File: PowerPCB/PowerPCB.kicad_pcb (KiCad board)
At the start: 2 copper layers, 41 parts, among them J1 Conn_01x03_Male, J2 Conn_01x10_Male, J5 Conn_01x07_Male, K1 1721081-5, K2 1721081-5, K3 1721081-5, Q1 Q_PMOS_DGS, U1 NCP1117-3.3_SOT223, U2 STM32F413ZHTx, U3 NCP1117-5.0_SOT223, U4 MCP2562-E-P, U5 MCP2562-E-P

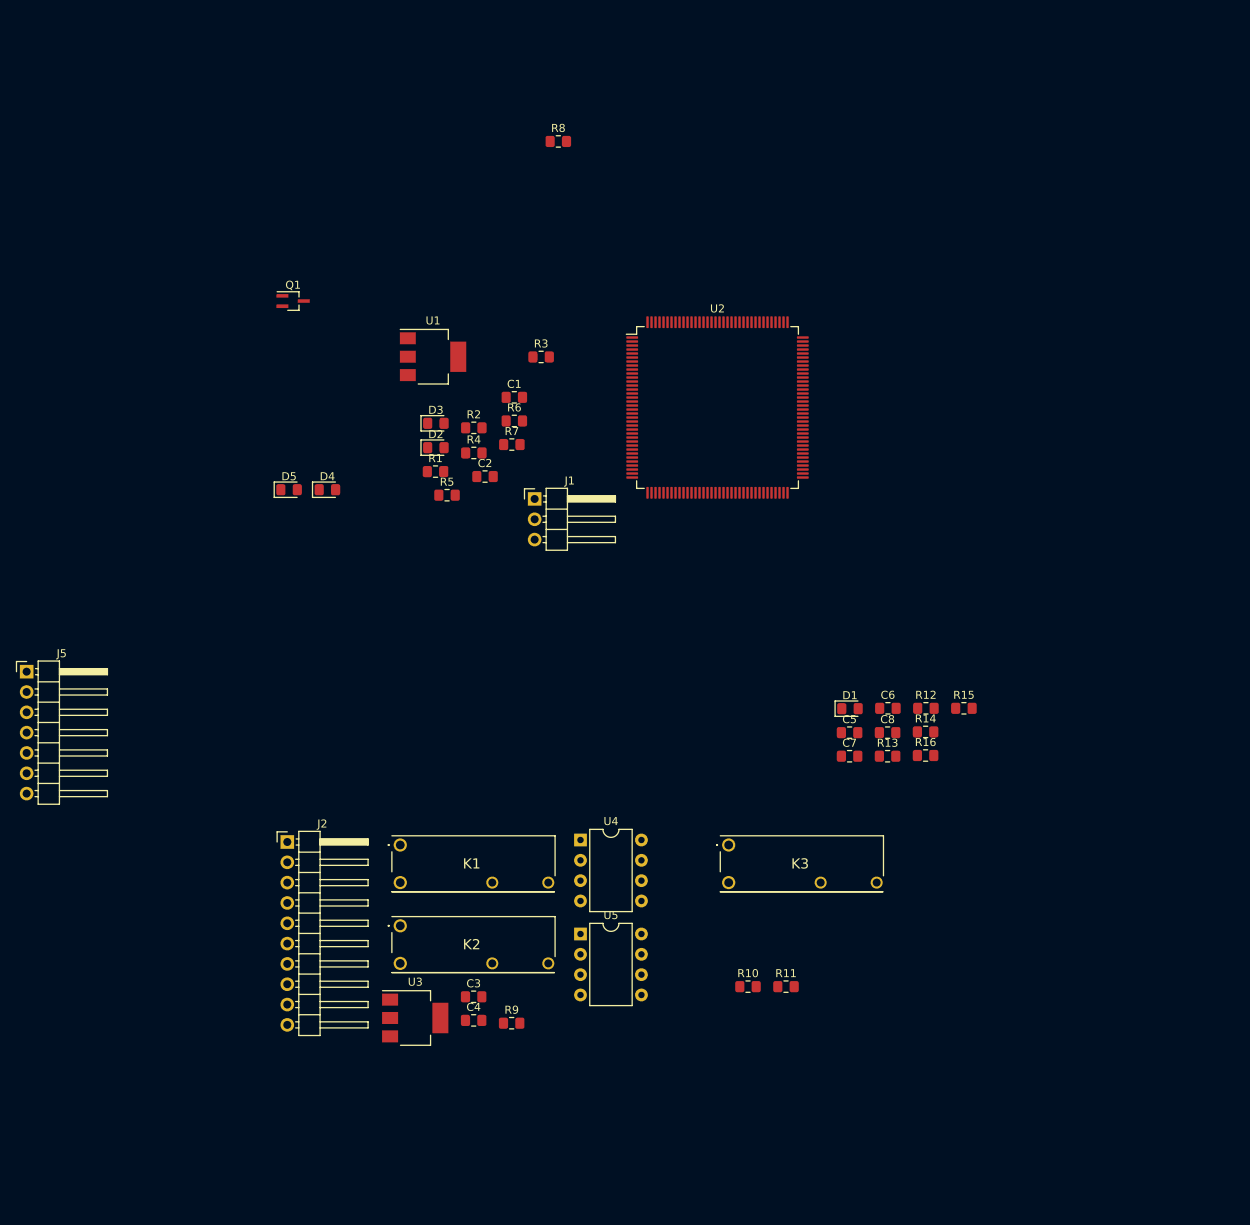
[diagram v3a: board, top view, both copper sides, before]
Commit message: Create new Daichi branch, made PCB layout up to the tracks
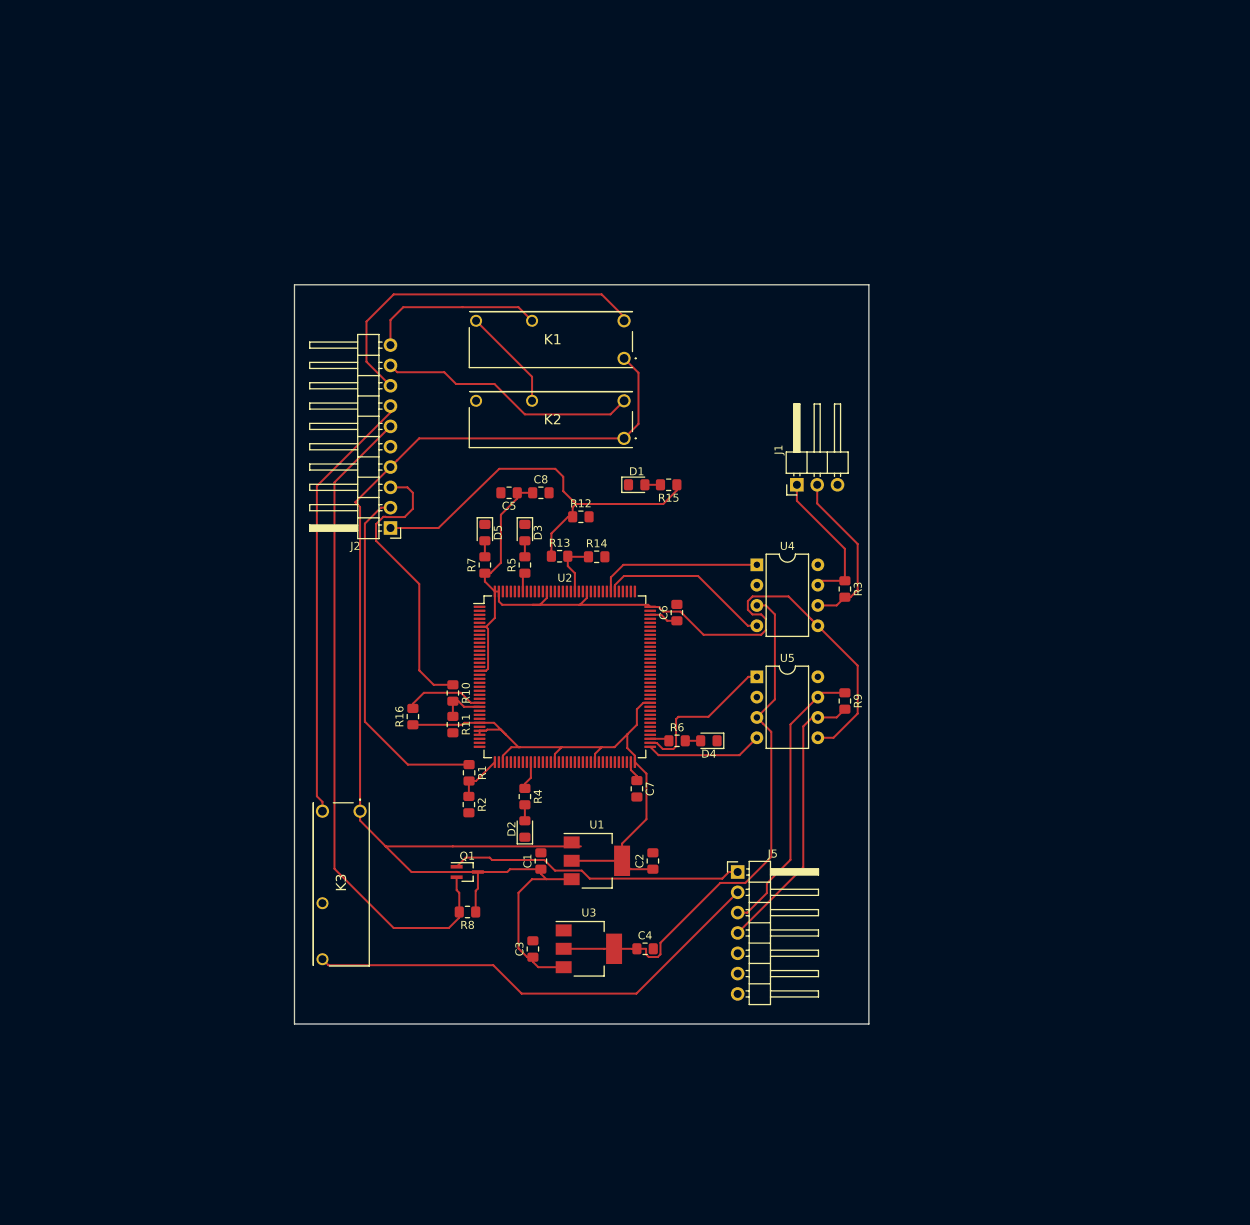
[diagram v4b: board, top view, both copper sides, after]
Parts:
- moved R8 97.0 mm to (354.8, 243.4), turned to 180 degrees
- moved J5 92.3 mm to (388.6, 238.4)
- moved Q1 74.6 mm to (354.8, 238.4)
- moved K2 67.0 mm to (374.4, 184.2), turned to 180 degrees
- moved K1 66.9 mm to (374.4, 174.2), turned to 180 degrees
- moved U1 66.3 mm to (371.0, 237.0)
- moved R16 64.3 mm to (348.0, 219.0), turned to 90 degrees
- moved C1 58.1 mm to (364.0, 237.0), turned to 90 degrees
- moved R9 57.9 mm to (402.0, 217.0), turned to 270 degrees
- moved D4 57.1 mm to (385.0, 222.0), turned to 180 degrees
- moved R11 53.0 mm to (353.0, 220.0), turned to 270 degrees
- moved C8 52.7 mm to (364.0, 191.0)
- moved C2 52.4 mm to (378.0, 237.0), turned to 90 degrees
- moved C5 52.1 mm to (360.0, 191.0), turned to 180 degrees
- moved R10 52.0 mm to (353.0, 216.0), turned to 270 degrees
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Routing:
- net VCC_3.3: track 0.00 -> 181.8 mm
- net VCC_12: track 0.00 -> 166.2 mm
- net /Fan/FanPWM: track 0.00 -> 82.6 mm
- net VCC_5: track 0.00 -> 67.5 mm
- net /Fan/Fan-: track 0.00 -> 58.9 mm
- net /Fan/FanCtrl: track 0.00 -> 54.7 mm
- net DCDC_ON: track 0.00 -> 51.2 mm
- net Net-(J2-Pad8): track 0.00 -> 44.5 mm
- net AUX+: track 0.00 -> 44.0 mm
- net /Fan/Fan+: track 0.00 -> 37.0 mm
- net DCDC+: track 0.00 -> 36.0 mm
- net MAIN_CAN_HI: track 0.00 -> 35.4 mm
- net MAIN_CAN_LO: track 0.00 -> 35.3 mm
- net Net-(J2-Pad9): track 0.00 -> 32.4 mm
- net Net-(J2-Pad10): track 0.00 -> 22.2 mm
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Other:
- board outline added: 71.8 x 92.4 mm

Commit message: small changes to tracks
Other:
- net class Default: trace_width 0.25 -> 1.27
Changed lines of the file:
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@@
   )
   (setup
-    (last_trace_width 0.25)
+    (last_trace_width 1.27)
     (trace_clearance 0.2)
     (zone_clearance 0.508)
@@
   (net_class Default "This is the default net class."
     (clearance 0.2)
-    (trace_width 0.25)
+    (trace_width 1.27)
     (via_dia 0.8)
     (via_drill 0.4)
@@
   (segment (start 374.4 184.2) (end 376.2 182.4) (width 0.25) (layer F.Cu) (net 2))
   (segment (start 376.2 182.4) (end 376.2 176) (width 0.25) (layer F.Cu) (net 2))
-  (segment (start 345.2 187.78) (end 340.8 192.18) (width 0.25) (layer F.Cu) (net 2))
   (segment (start 362.9 239.3) (end 364.675 239.3) (width 0.25) (layer F.Cu) (net 2))
   (segment (start 361.2 241) (end 362.9 239.3) (width 0.25) (layer F.Cu) (net 2))
@@
   (segment (start 356.13 238.4) (end 359.8 238.4) (width 0.25) (layer F.Cu) (net 2))
   (segment (start 359.8 238.4) (end 360.15 238.05) (width 0.25) (layer F.Cu) (net 2))
-  (segment (start 341.4 192.78) (end 341.4 230.8) (width 0.25) (layer F.Cu) (net 2))
-  (segment (start 340.8 192.18) (end 341.4 192.78) (width 0.25) (layer F.Cu) (net 2))
   (segment (start 374.4 184.2) (end 348.78 184.2) (width 0.25) (layer F.Cu) (net 2))
   (segment (start 346.049999 186.930001) (end 345.2 187.78) (width 0.25) (layer F.Cu) (net 2))
   (segment (start 348.78 184.2) (end 346.049999 186.930001) (width 0.25) (layer F.Cu) (net 2))
+  (segment (start 340.8 230.2) (end 341.4 230.8) (width 0.25) (layer F.Cu) (net 2))
+  (segment (start 345.2 187.78) (end 340.8 192.18) (width 0.25) (layer F.Cu) (net 2))
+  (segment (start 340.8 192.18) (end 340.8 230.2) (width 0.25) (layer F.Cu) (net 2))
   (segment (start 362 230) (end 362 232) (width 0.25) (layer F.Cu) (net 3))
   (segment (start 362 197) (end 362 199) (width 0.25) (layer F.Cu) (net 4))

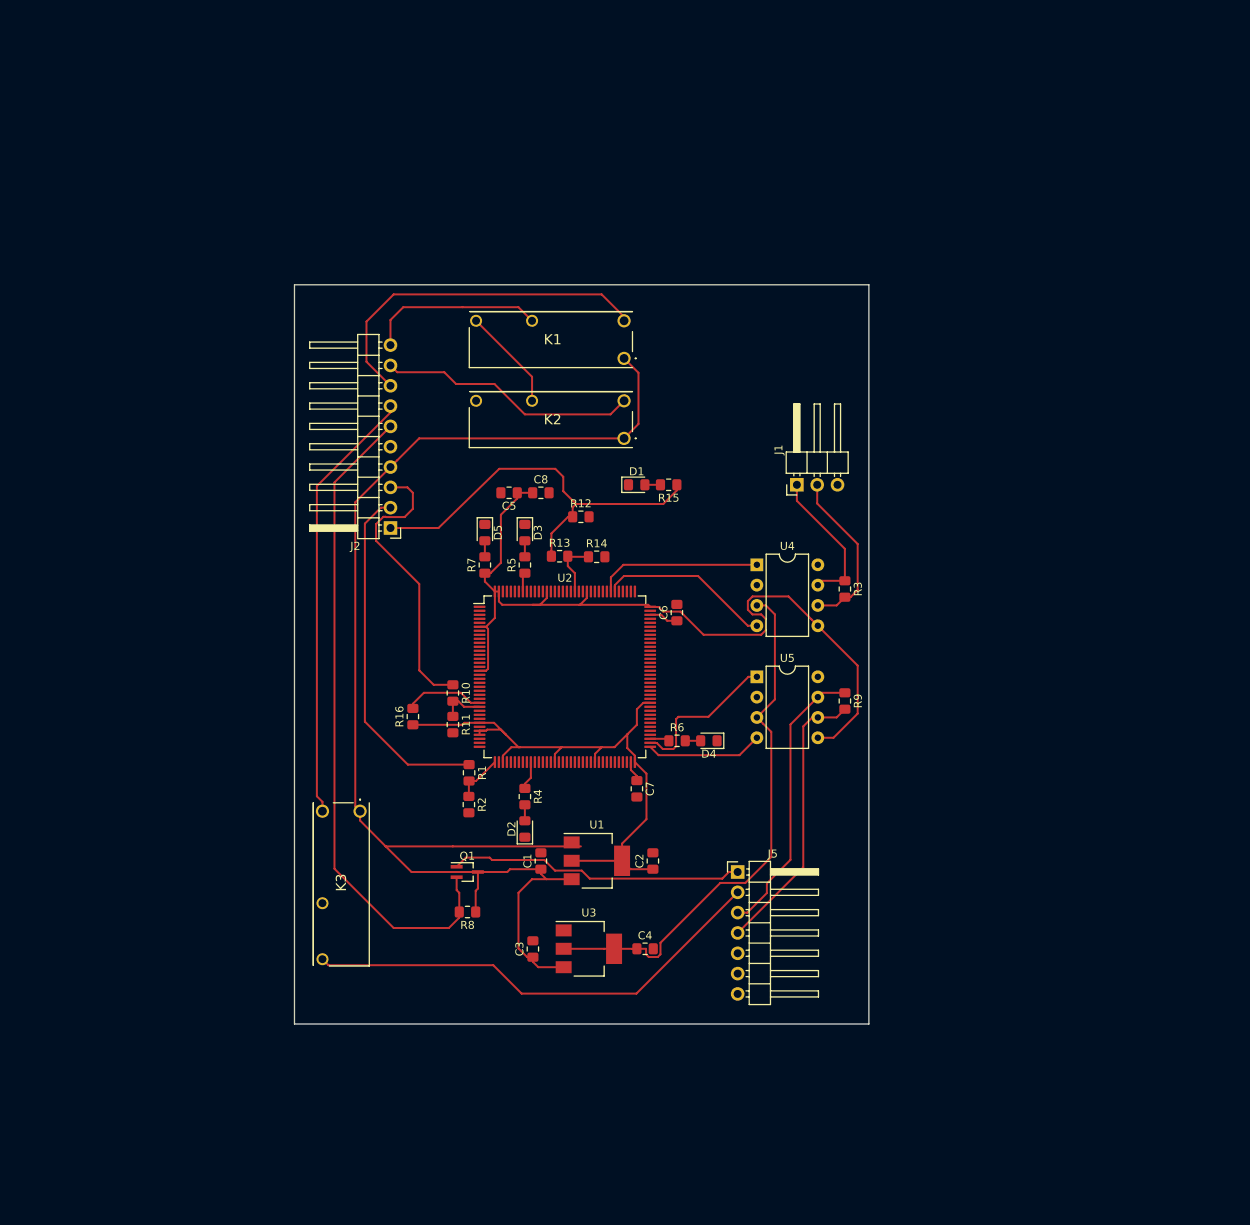
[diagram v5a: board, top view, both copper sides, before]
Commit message: cleared up rats nest more and keep LEDs together
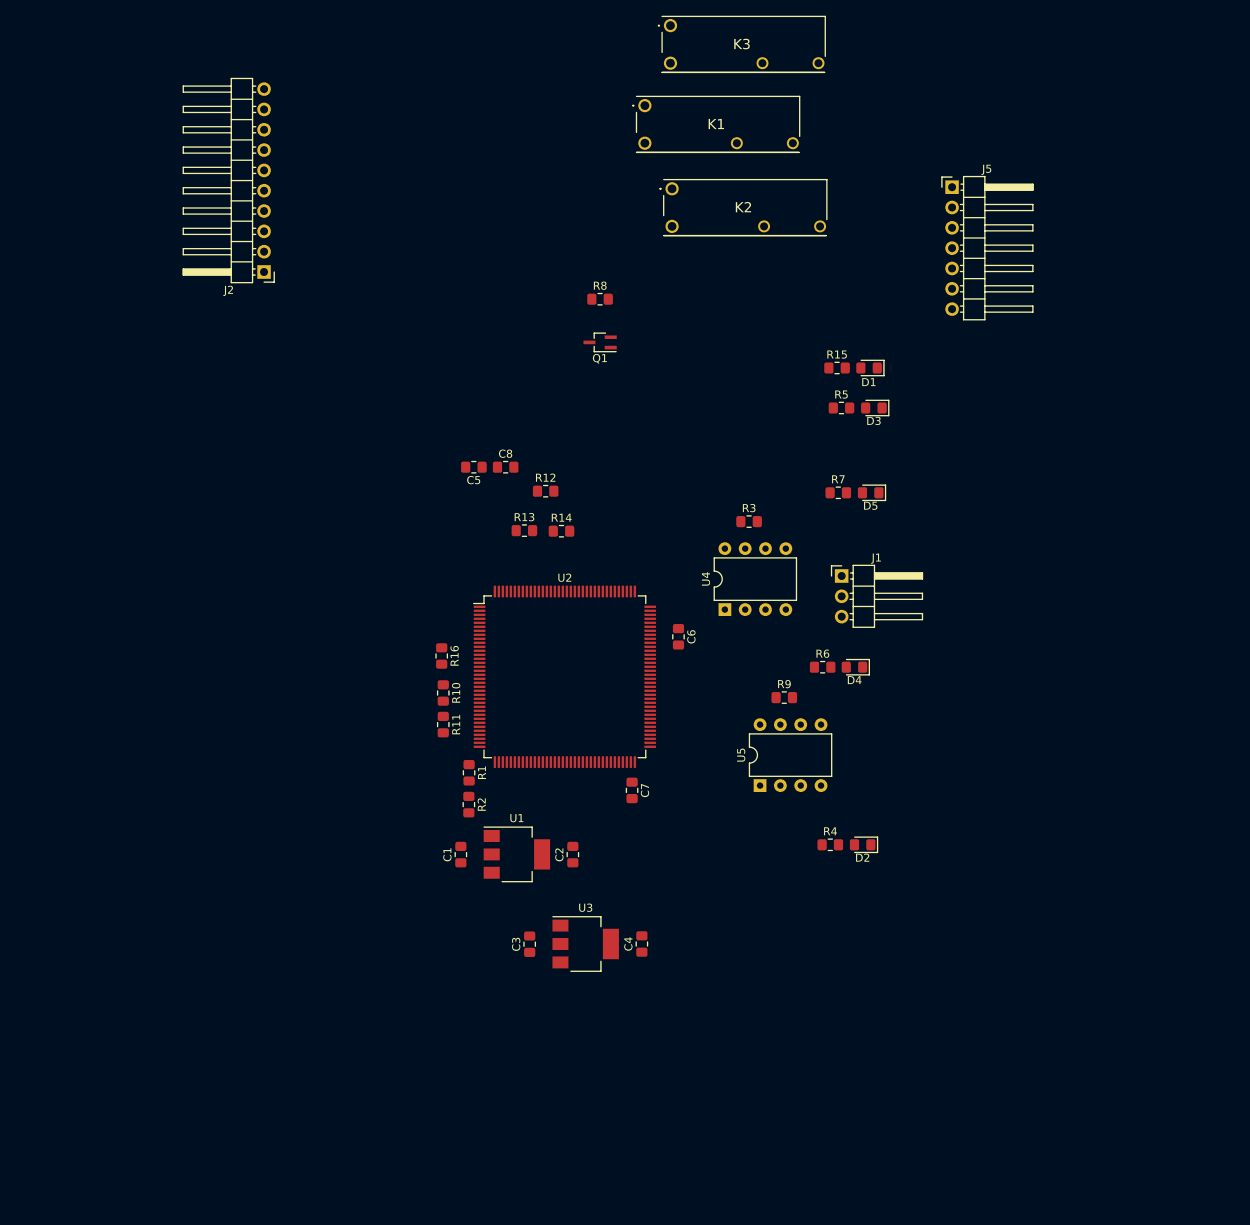
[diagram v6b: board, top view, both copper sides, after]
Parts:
- moved K3 105.6 mm to (380.2, 132.6), turned to 0 degrees
- moved J5 89.7 mm to (415.4, 152.8)
- moved R8 78.4 mm to (371.4, 166.8), turned to 0 degrees
- moved Q1 68.2 mm to (371.4, 172.2), turned to 180 degrees
- moved D5 48.5 mm to (405.2, 191.0), turned to 180 degrees
- moved D3 46.3 mm to (405.6, 180.4), turned to 180 degrees
- moved R7 45.1 mm to (401.2, 191.0), turned to 0 degrees
- moved R5 44.2 mm to (401.6, 180.4), turned to 0 degrees
- moved D2 42.3 mm to (404.2, 235.0), turned to 180 degrees
- moved R4 38.6 mm to (400.2, 235.0), turned to 0 degrees
- moved J2 35.7 mm to (329.4, 163.4)
- moved D1 32.5 mm to (405.0, 175.4), turned to 180 degrees
- moved K2 31.8 mm to (380.4, 153.0), turned to 0 degrees
- moved K1 31.7 mm to (377.0, 142.6), turned to 0 degrees
- moved R15 25.6 mm to (401.0, 175.4), turned to 0 degrees
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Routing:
- net VCC_3.3: track 181.8 -> 0.00 mm
- net VCC_12: track 166.2 -> 0.00 mm
- net /Fan/FanPWM: track 82.6 -> 0.00 mm
- net VCC_5: track 67.5 -> 0.00 mm
- net /Fan/Fan-: track 58.9 -> 0.00 mm
- net /Fan/FanCtrl: track 54.7 -> 0.00 mm
- net DCDC_ON: track 51.2 -> 0.00 mm
- net Net-(J2-Pad8): track 44.5 -> 0.00 mm
- net AUX+: track 44.0 -> 0.00 mm
- net /Fan/Fan+: track 37.0 -> 0.00 mm
- net DCDC+: track 36.0 -> 0.00 mm
- net MAIN_CAN_HI: track 35.4 -> 0.00 mm
- net MAIN_CAN_LO: track 35.3 -> 0.00 mm
- net Net-(J2-Pad9): track 32.4 -> 0.00 mm
- net Net-(J2-Pad10): track 22.2 -> 0.00 mm
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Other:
- board outline removed
- net class Default: trace_width 1.27 -> 0.762
